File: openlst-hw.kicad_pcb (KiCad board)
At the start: 4 copper layers, 50 x 43 mm, 98 parts, among them J1 Battery, J2 CC Prog/Debug, J3 UART0, J4 SPI0, J5 Control Outputs, J6 ANT, U1 LP2981-3.3, U2 CC1110, U3 AP6502, U4 ASFL1-27.000MHZ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

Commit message: changed connectors, halfway through pcb
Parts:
- removed J1: Battery, TerminalBlock_Phoenix:TerminalBlock_Phoenix_MKDS-1,5-2-5.08_1x02_P5.08mm_Horizontal
- removed U9: RFFM6404, openlst:Qorvo_LGA_28_ThermalVias
- added J3: Conn_02x10_Odd_Even, satfab_3rdparty:ERM8-010-YY.Y-XXX-DV-TR, F.Cu at (155.3, 125.5)
- added U7: RFFM6406, openlst:Qorvo_LGA_28_ThermalVias, F.Cu at (173.8, 87.4)
- J6: footprint Connector_Coaxial:SMA_Samtec_SMA-J-P-X-ST-EM1_EdgeMount -> satfab_3rdparty:SAMTEC_MMCXV-J-P-HF-ST-TH1
- moved J6 0.86 mm to (184.3, 85.4), turned to 0 degrees
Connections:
- R5 pad 2: /CAN_CS -> /UART1_CTS
- R6 pad 2: /CAN_SCK -> /UART1_RTS
- R7 pad 2: /CAN_MOSI -> /UART1_TX
- R8 pad 2: /CAN_MISO -> /UART1_RX
- U2 pad 1: Net-(R9-Pad1) -> unconnected-(U2-P1_2-Pad1)
- U2 pad 36: Net-(R10-Pad1) -> unconnected-(U2-P1_3-Pad36)
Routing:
- net GND: track 107.5 -> 94.0 mm, vias 98 -> 91
- net /VAA_FILT: track 11.4 -> 14.1 mm
- net Net-(J6-In): track 5.06 -> 4.01 mm
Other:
- board text removed: "BATT"
- board text removed: "GND"

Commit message: finished edits v1
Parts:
- removed C12: 0.1u, Capacitor_SMD:C_0603_1608Metric
- removed C13: 0.01u, Capacitor_SMD:C_0603_1608Metric
- removed C14: 6.8n, Capacitor_SMD:C_0603_1608Metric
- removed C15, C16: 22u, Capacitor_SMD:C_1210_3225Metric
- removed C17, C18, C4: 10u, Capacitor_SMD:C_0805_2012Metric
- removed J2: CC Prog/Debug, Connector_PinHeader_1.27mm:PinHeader_2x05_P1.27mm_Vertical_SMD
- removed the J3 at (159.9, 75.4)
- removed J4: SPI0, Connector_PinHeader_2.54mm:PinHeader_1x06_P2.54mm_Vertical
- removed J5: Control Outputs, Connector_PinHeader_2.54mm:PinHeader_1x03_P2.54mm_Vertical
- removed L1: 10u, Inductor_SMD:L_Vishay_IFSC-1515AH_4x4x1.8mm
- removed R10, R13, R14, R9: 100, Resistor_SMD:R_0603_1608Metric
- removed R15: 6k8, Resistor_SMD:R_0603_1608Metric
- removed R19: 36k, Resistor_SMD:R_0603_1608Metric
- removed R20: 10k, Resistor_SMD:R_0603_1608Metric
- removed U1: LP2981-3.3, Package_TO_SOT_SMD:SOT-23-5
- removed U3: AP6502, openlst:SOIC-8-1EP_3.9x4.9mm_P1.27mm_EP2.613x3.502mm
- removed kibuzzard-610AE595: G***, kibuzzard-610AE595
- removed kibuzzard-610AE658: G***, kibuzzard-610AE658
- removed kibuzzard-610AE73D (x3): G***, kibuzzard-610AE73D
- removed kibuzzard-610AE761: G***, kibuzzard-610AE761
- removed kibuzzard-610AE773: G***, kibuzzard-610AE773
- removed kibuzzard-610AE8D4: G***, kibuzzard-610AE8D4
- removed kibuzzard-610AE8E6: G***, kibuzzard-610AE8E6
- removed kibuzzard-610AE965: G***, kibuzzard-610AE965
- removed kibuzzard-610AE972: G***, kibuzzard-610AE972
- removed kibuzzard-610AE9EB: G***, kibuzzard-610AE9EB
- removed kibuzzard-610AEA01: G***, kibuzzard-610AEA01
- added TP1: TestPoint, satfab:RCUCTE_0603_Test_Point, F.Cu at (149.1, 77.9)
- added TP2: TestPoint, satfab:RCUCTE_0603_Test_Point, F.Cu at (150.8, 77.9)
- moved R21 34.9 mm to (146.3, 85.3)
- moved R22 34.9 mm to (146.3, 82.0)
- moved J3 31.6 mm to (174.3, 100.3)
- moved R8 19.3 mm to (165.1, 97.4), turned to -90 degrees
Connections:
- J3 pad 10: /UART_RX_0 -> /UART_CTS_1
- J3 pad 12: /UART_CTS_0 -> /~{LST_RESET}
- J3 pad 14: /~{LST_RESET} -> /UART_RX_1
- J3 pad 16: /PROG_DC -> /PROG_DD
- J3 pad 18: /PROG_DD -> /PROG_DC
- J3 pad 6: /UART_RTS_0 -> /UART_TX_1
- J3 pad 8: /UART_TX_0 -> /UART_RTS_1
- R5 pad 2: /UART1_CTS -> /UART_CTS_1
- R6 pad 2: /UART1_RTS -> /UART_RTS_1
- R7 pad 2: /UART1_TX -> /UART_TX_1
- R8 pad 2: /UART1_RX -> /UART_RX_1
- U2 pad 6: /AN1 -> unconnected-(U2-P0_1-Pad6)
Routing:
- net /UART_CTS_1: track 0.00 -> 37.0 mm, vias 0 -> 2
- net /UART_RTS_1: track 0.00 -> 35.9 mm, vias 0 -> 2
- net VAA: track 6.07 -> 41.9 mm, vias 5 -> 3
- net /UART_TX_1: track 0.00 -> 34.3 mm, vias 0 -> 2
- net /AN0: track 39.8 -> 7.88 mm, vias 2 -> 0
- net +BATT: track 24.8 -> 0.00 mm, vias 2 -> 0
- net /UART0_RTS: track 16.4 -> 0.00 mm
- net GND: track 94.0 -> 78.3 mm, vias 91 -> 78
- net Net-(U3-BST): track 15.1 -> 0.00 mm, vias 2 -> 0
- net /PROG_DC: track 15.3 -> 28.9 mm
- net /UART_RX_1: track 0.00 -> 12.7 mm
- net Net-(U2-P0_5): track 6.08 -> 16.5 mm
- net /~{LST_RESET}: track 5.50 -> 15.2 mm
- net /UART0_TX: track 11.3 -> 2.42 mm
- net +3V3: track 26.8 -> 18.5 mm
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- removed copper zone on F.Cu, net +BATT
- removed copper zone on F.Cu, net Net-(U3-SW)
- removed copper zone on F.Cu, net VAA
- removed copper zone on In2.Cu, net VAA

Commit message: finished edits v2
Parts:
- H1, H2, H3, H4: footprint MountingHole:MountingHole_3.2mm_M3 -> MountingHole:MountingHole_3.2mm_M3_Pad_Via
- J3: moved to B.Cu
- L2: footprint Inductor_SMD:L_0603_1608Metric -> Inductor_SMD:L_1206_3216Metric
- moved H3 45.2 mm to (141.0, 90.5)
- moved H4 45.1 mm to (183.5, 90.5)
- moved L2 13.8 mm to (167.8, 105.0), turned to 0 degrees
- moved R8 12.1 mm to (165.5, 109.5)
- moved C1 12.1 mm to (150.0, 105.5)
- moved C10 12.1 mm to (158.3, 95.0)
- moved C11 12.1 mm to (169.3, 96.5)
- moved C19 12.1 mm to (153.0, 93.2)
- moved C2 12.1 mm to (155.3, 105.0)
- moved C21 12.1 mm to (159.8, 103.0)
- moved C22 12.1 mm to (158.8, 105.5)
- moved C23 12.1 mm to (158.8, 98.0)
- moved C24 12.1 mm to (158.8, 101.0)
- moved C25 12.1 mm to (159.8, 100.0)
- moved C26 12.1 mm to (163.3, 96.5)
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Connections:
- J3 pad 10: /UART_CTS_1 -> /UART_RX_1
- J3 pad 14: /UART_RX_1 -> /UART_CTS_1
- J3 pad 16: /PROG_DD -> /UART_RTS_1
- J3 pad 18: /PROG_DC -> /UART_TX_1
- J3 pad 6: /UART_TX_1 -> /PROG_DC
- J3 pad 8: /UART_RTS_1 -> /PROG_DD
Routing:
- net VAA: track 41.9 -> 25.4 mm, vias 3 -> 2
- net /UART_RX_1: track 12.7 -> 6.83 mm, vias 0 -> 1
- net /UART_CTS_1: track 37.0 -> 31.4 mm, vias 2 -> 1
- net /PROG_DD: track 28.6 -> 23.4 mm, vias 2 -> 1
- net /UART_RTS_1: track 35.9 -> 30.6 mm, vias 2 -> 1
- net /~{LST_RESET}: track 15.2 -> 10.0 mm, vias 0 -> 1
- net /PROG_DC: track 28.9 -> 24.5 mm, vias 2 -> 1
- net /UART_TX_1: track 34.3 -> 30.7 mm, vias 2 -> 1
- net GND: track 78.3 -> 80.7 mm, vias 78 -> 79
- net /VAA_FILT: track 14.1 -> 15.9 mm
- net +3V3: track 18.5 -> 19.5 mm
- added copper zone on B.Cu, net GND
- added copper zone on B.Cu, net VAA
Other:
- board size 50 x 43 mm -> 50 x 28.7 mm
- board text added: "2023-12-18 Abi Guicheteau"
- board text added: "OpenLST v3.0"
- board text removed: "OpenLST v2.5"

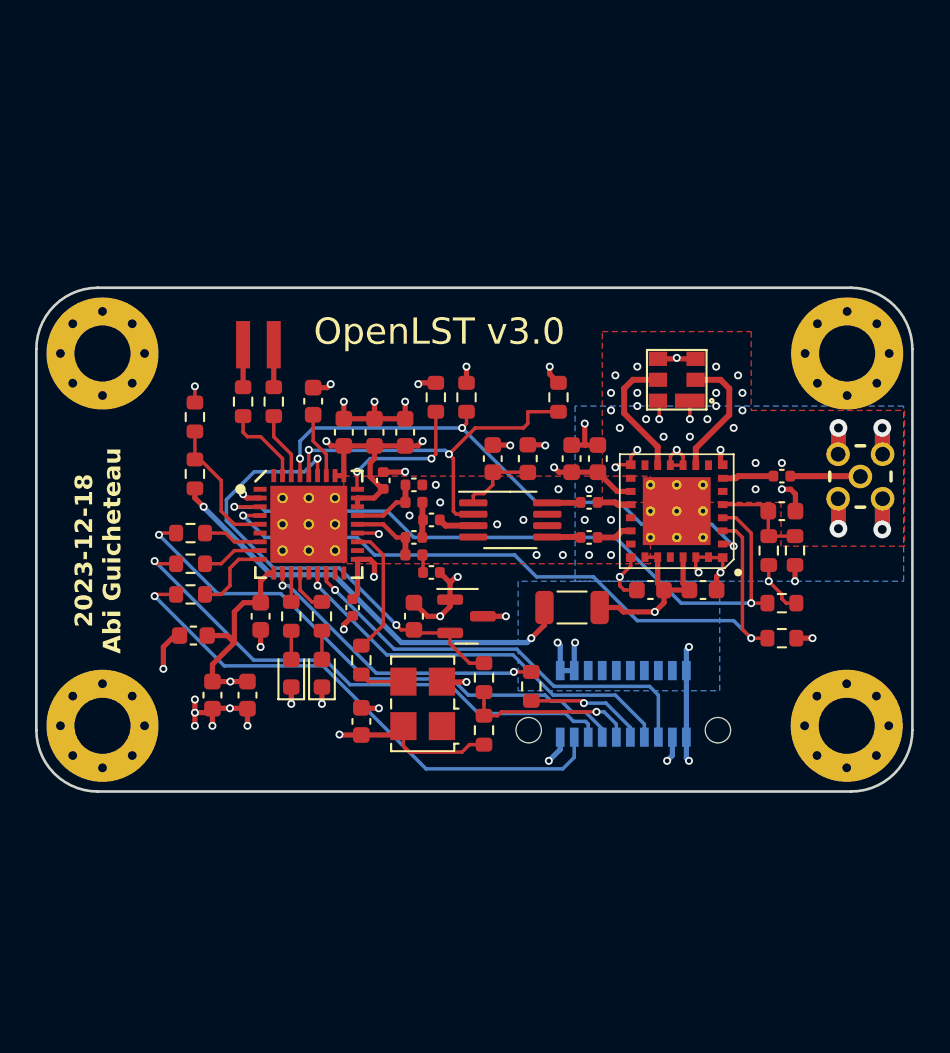
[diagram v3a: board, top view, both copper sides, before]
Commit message: fixed rf connection and power lines
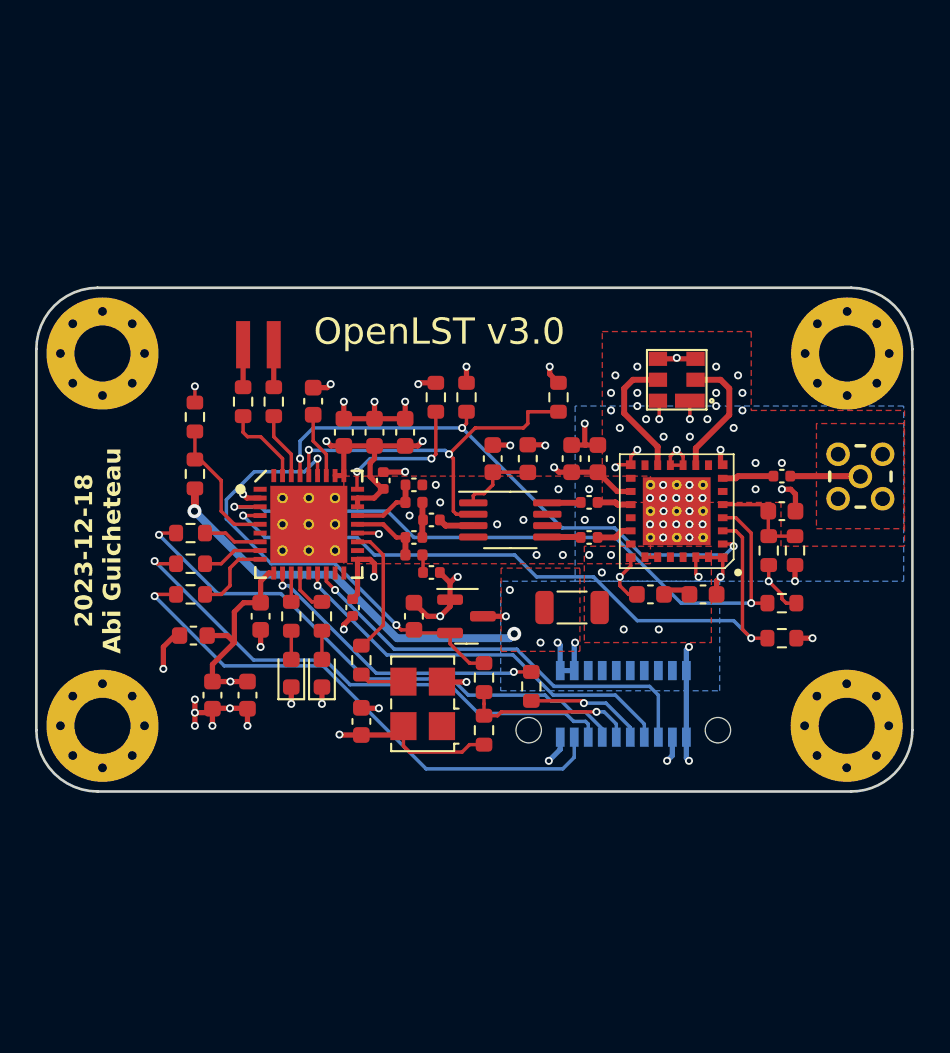
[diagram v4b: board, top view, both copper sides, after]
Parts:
- moved C46 0.25 mm to (175.3, 104.2)
- moved C8 0.25 mm to (172.3, 104.2)
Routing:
- net GND: track 80.7 -> 68.6 mm, vias 79 -> 91
- net /VAA_FILT: track 15.9 -> 7.12 mm, vias 2 -> 4
- net VAA: track 25.4 -> 22.7 mm, vias 2 -> 4
- added copper zone on F.Cu, net /VAA_FILT
- added copper zone on F.Cu, net VAA
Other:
- board size 50 x 28.7 mm -> 50 x 28.8 mm

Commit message: rotated ferrite bead and added 3d models
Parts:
- moved L2 1.97 mm to (169.5, 106.0), turned to 90 degrees
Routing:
- net VAA: track 22.7 -> 25.1 mm, vias 4 -> 6
- net GND: track 68.6 -> 67.8 mm
- net /VAA_FILT: vias 4 -> 6
